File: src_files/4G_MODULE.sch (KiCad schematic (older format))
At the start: 28 parts

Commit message: schematic capture complete
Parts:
- removed AE? (x2): Antenna_Shield, symbol Device:Antenna_Shield
- added J12: DEBUG_4G, Connector_PinHeader_2.54mm:PinHeader_1x02_P2.54mm_Vertical, symbol Connector:Conn_01x02_Male
- added J13, J14: U.FL-R-SMT-1(10), greencharge-footprints:HRS_U.FL-R-SMT-1(10), symbol U.FL-R-SMT-1_10_:U.FL-R-SMT-1(10)
- C226, C230: renamed from C?; footprint (none) -> Capacitor_SMD:CP_Elec_5x5.4
- C227, C228, C229, C231, C232, C233, C234, C235, C236, C237: renamed from C?; footprint (none) -> Capacitor_SMD:C_0402_1005Metric
- D20: renamed from D?; footprint (none) -> LED_SMD:LED_0603_1608Metric
- J9: renamed from J?; footprint (none) -> greencharge-footprints:MOLEX_78800-0001
- R79, R80, R81, R82, R83: renamed from R?; footprint (none) -> Resistor_SMD:R_0402_1005Metric
- U19: renamed from U?; footprint (none) -> greencharge-footprints:XCVR_EG91EFB-512-SNND
- gave numbers to parts that had none: 6
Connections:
- wire segments 176 -> 182
- no-connect marks 7 -> 59
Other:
- moved on the sheet: C234, C235, C236, C237, R81, R82, R83, U20

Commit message: updated footprint and schematics
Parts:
- removed J12: DEBUG_4G, Connector_PinHeader_2.54mm:PinHeader_1x02_P2.54mm_Vertical, symbol Connector:Conn_01x02_Male
- removed J9: SIM_Card, greencharge-footprints:MOLEX_78800-0001, symbol New_Connector:SIM_Card
- removed U19: quesctel_EG91-EX, greencharge-footprints:XCVR_EG91EFB-512-SNND, symbol GCL_Integrated-Circuits:quesctel_EG91-EX
- added C284, C285: 10nF, Capacitor_SMD:C_0402_1005Metric, symbol Device:C_Small
- added D26: SMF11A, Diode_SMD:D_SOD-123, symbol dk_TVS-Diodes:ESD5Z3_3T1G
- added D27: LED_GREEN, LED_SMD:LED_0603_1608Metric, symbol Device:LED
- added J9: SIM_Card_Shielded, greencharge-footprints:GCT_SIM8066-6-1-14-01-A_REVA, symbol Connector:SIM_Card_Shielded
- added JP1: Jumper, TestPoint:TestPoint_2Pads_Pitch2.54mm_Drill0.8mm, symbol Device:Jumper
- added Q12: DTC143ZEBTL, greencharge-footprints:SOTFL50P160X85-3N, symbol DTC143ZEBTL:DTC143ZEBTL
- added R106, R107, R108: 4.7K, Resistor_SMD:R_0402_1005Metric, symbol Device:R_US
- added R109: 0R, Resistor_SMD:R_0402_1005Metric, symbol Device:R_US
- added TP20, TP21: DBG_RXD, TestPoint:TestPoint_Pad_2.0x2.0mm, symbol Connector:TestPoint
- added U19: EG25G, greencharge-footprints:XCVR_EG25G, symbol EG25G:EG25G
- C226, C230: footprint Capacitor_SMD:CP_Elec_5x5.4 -> Capacitor_Tantalum_SMD:CP_EIA-3216-18_Kemet-A; MPN (none) -> T490A107M006ATE800
- D20: value LED -> LED_GREEN
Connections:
- net labels added: 1.8V_local_ldo, ANT_GNSS_GPS, ANT_MAIN, AP_READY, DBG_RXD, DBG_TXD, Net_status, PWR_EN, RESET_n, Status_indicator, USB_BOOT
- wire segments 182 -> 154
- no-connect marks 59 -> 47
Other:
- note added: "50 ohm IMPEDANCE LINES"
- note added: "ANTENNAS(4G LTE AND GPS)"
- note added: "CODEC_INTERFACE"
- note added: "EG25G 4G(LTE/GSM) AND GPS MODULE"
- note added: "ESD PROTECTION FOR USB LINES"
- note added: "GPS ANTENNA = PASSIVE\nFRQ= 1575.42±1.023"
- note added: "LTE_CAPABLE ANTENNA\nFRQ= TX=1920~1980 \n RX= 2110~2170"
- note added: "MODULE ENABLE CIRCUIT"
- note added: "NANO_SIM_CONNECTOR(8-pins)"
- note added: "NETWORK INDICATOR"
- note added: "RESET CIRCUIT"
- note added: "STATUS INDICATOR\n"
- note added: "Status Indicato"
- note added: "USB BOOT"
- note added: "pull_up"
- note removed: "NOTE: Ensure proper heat decipation"
- moved on the sheet: C226, C227, C228, C229, C230, C231, C232, C233, C234, C235, C236, C237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

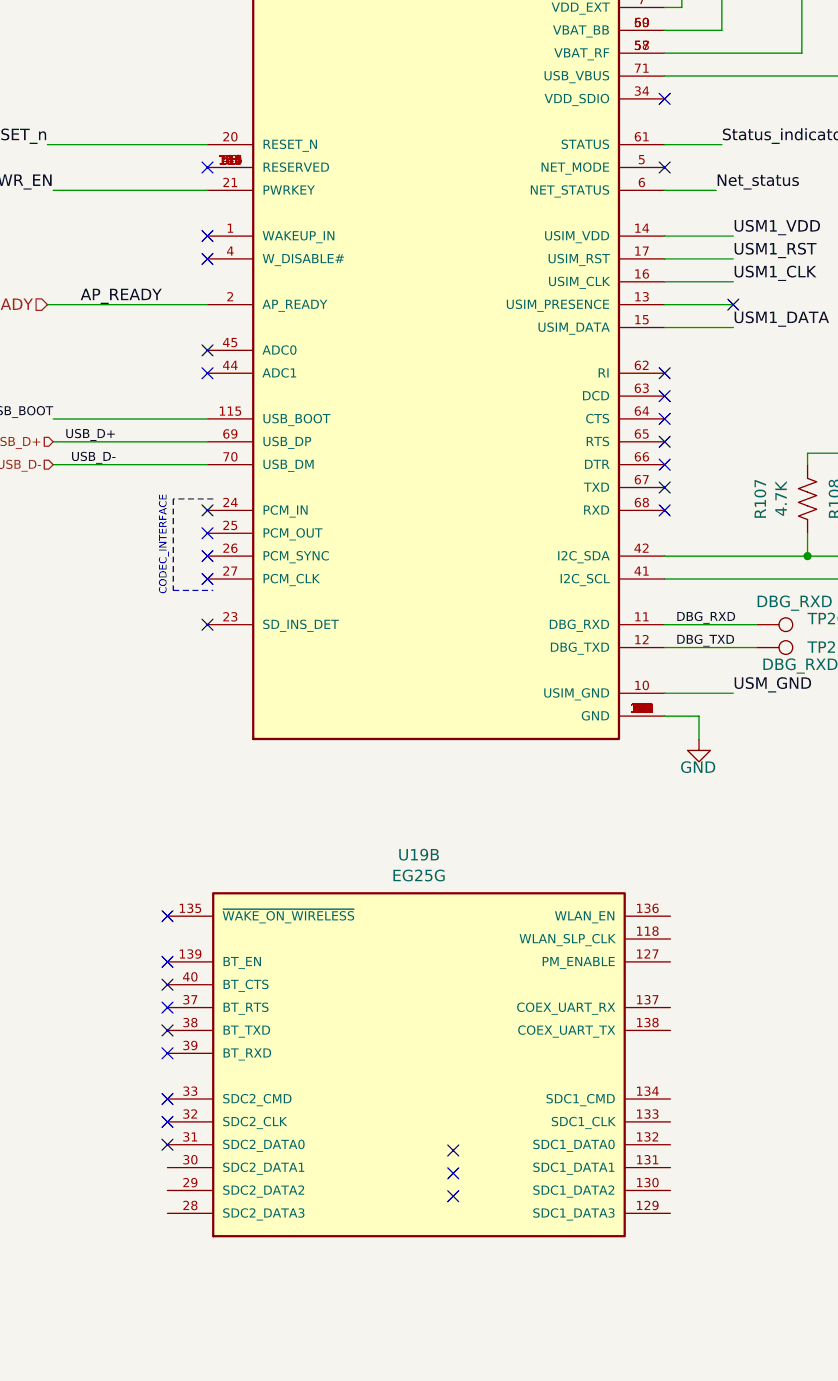
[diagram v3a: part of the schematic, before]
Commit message: complete update on schematic and all display interfaces
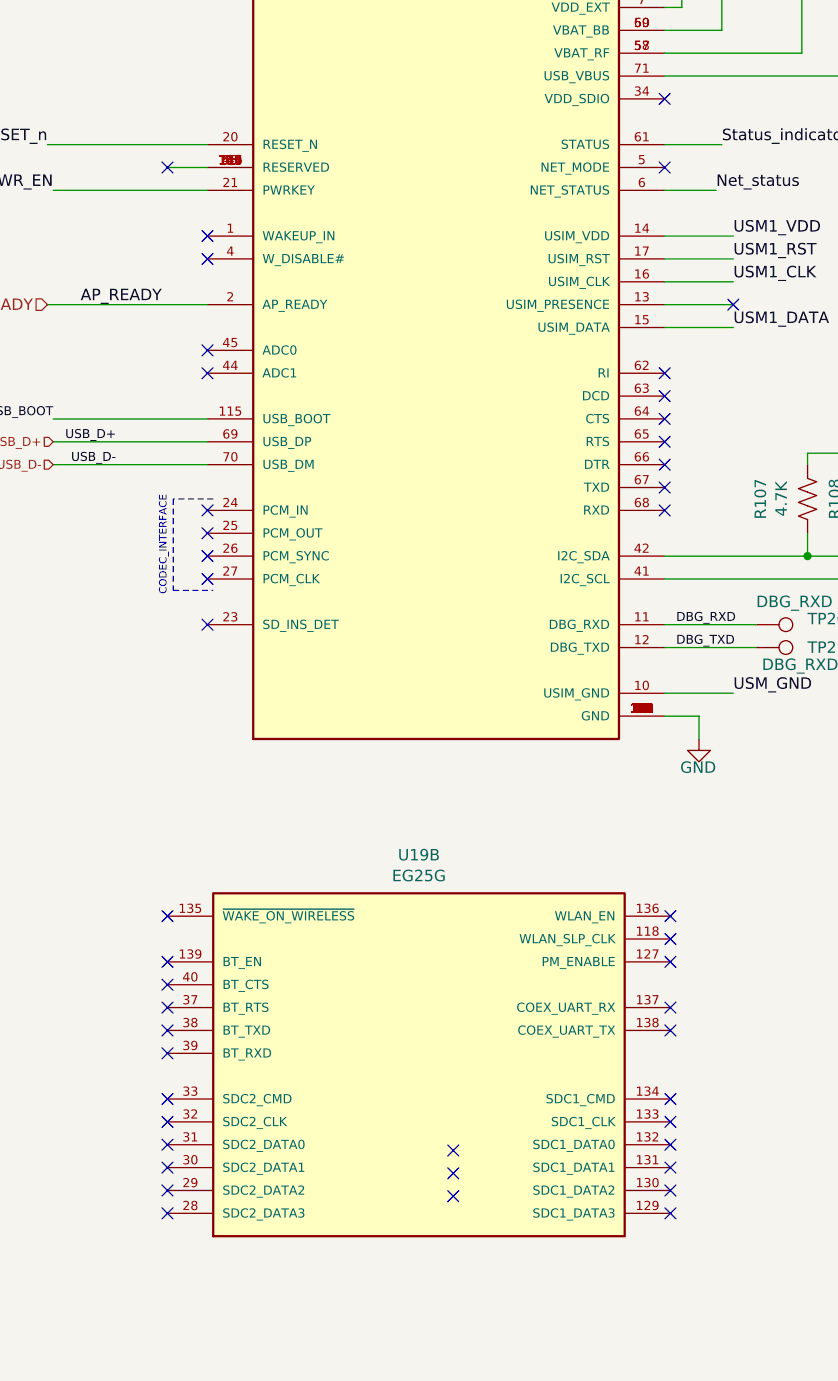
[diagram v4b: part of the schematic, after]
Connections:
- no-connect marks 47 -> 61
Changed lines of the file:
@@
 $Descr A3 16535 11693
 encoding utf-8
-Sheet 15 15
+Sheet 13 15
 Title ""
 Date ""
@@
 Wire Wire Line
 	5475 3300 4800 3300
-NoConn ~ 5475 3200
 Text GLabel 8400 2600 1    33   Input ~ 0
 VCC_3V3
@@
 	0    1    1    0
 $EndComp
+NoConn ~ 7500 6475
+NoConn ~ 7500 6575
+NoConn ~ 7500 6675
+NoConn ~ 7500 6875
+NoConn ~ 7500 6975
+NoConn ~ 7500 7275
+NoConn ~ 7500 7375
+NoConn ~ 7500 7475
+NoConn ~ 7500 7575
+NoConn ~ 7500 7675
+NoConn ~ 7500 7775
+NoConn ~ 5300 7575
+NoConn ~ 5300 7675
+NoConn ~ 5300 7775
+Wire Wire Line
+	5475 3200 5300 3200
+NoConn ~ 5300 3200
 $EndSCHEMATC

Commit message: complete update on schematiC + FOOTPRINT
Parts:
- removed J9: SIM_Card_Shielded, greencharge-footprints:GCT_SIM8066-6-1-14-01-A_REVA, symbol Connector:SIM_Card_Shielded
- added J9: SIM8066-6-1-14-01-A_REVA, greencharge-footprints:GCT_SIM8066-6-1-14-01-A_REVA, symbol SIM8066-6-1-14-01-A_REVA:SIM8066-6-1-14-01-A_REVA
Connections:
- net USM_GND is gone; now on net GND: C236.1, U19.10 (USIM_GND)
- net GND: now also J9.C5 (GND), J9.CD, J9.G1 (GND), J9.G2 (GND), J9.G3 (GND), J9.G4 (GND)
- net USM1_VDD: now also J9.C1 (VCC)
- net at C234.1, R109.1, R81.1: now also J9.C7 (I/O)
- net at C237.1, R82.1: now also J9.C2 (RST)
- net at C235.1, R83.1: now also J9.C3 (CLK)
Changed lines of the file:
@@
 Wire Wire Line
 	7475 3500 7775 3500
-Text Label 12550 7375 2    50   ~ 0
+Text Label 12325 7375 2    50   ~ 0
 USM_GND
 Text Label 12575 7075 2    50   ~ 0
@@
 Wire Wire Line
 	13800 7275 14700 7275
-Wire Wire Line
-	12550 7375 14700 7375
 NoConn ~ 14700 7475
 Wire Wire Line
@@
 Text Notes 12075 6575 0    39   ~ 0
 NOTE: Keep placement of (U)SIM card connector to the module as close as possible. Keep the trace length\nas less than 200mm as possible.\nKeep (U)SIM card signals away from RF and VBAT traces.\nMINIMIZE cross talk.
-$Comp
-L Connector:SIM_Card_Shielded J9
-U 1 1 6305C88F
-P 15200 7375
-F 0 "J9" H 15275 6900 50  0000 L CNN
-F 1 "SIM_Card_Shielded" H 14925 6800 50  0000 L CNN
-F 2 "greencharge-footprints:GCT_SIM8066-6-1-14-01-A_REVA" H 15200 7725 50  0001 C CNN
-F 3 " ~" H 15150 7375 50  0001 C CNN
-	1    15200 7375
-	1    0    0    -1
-$EndComp
 Wire Wire Line
 	14575 7675 14575 8275
@@
 	5475 3200 5300 3200
 NoConn ~ 5300 3200
+$Comp
+L SIM8066-6-1-14-01-A_REVA:SIM8066-6-1-14-01-A_REVA J9
+U 1 1 6EC1A329
+P 15100 7375
+F 0 "J9" H 15330 7421 50  0000 L CNN
+F 1 "SIM8066-6-1-14-01-A_REVA" H 14625 7850 50  0000 L CNN
+F 2 "greencharge-footprints:GCT_SIM8066-6-1-14-01-A_REVA" H 15100 7375 50  0001 L BNN
+F 3 "" H 15100 7375 50  0001 L BNN
+F 4 "Manufacturer recommendations" H 15100 7375 50  0001 L BNN "STANDARD"
+F 5 "1.44mm" H 15100 7375 50  0001 L BNN "MAXIMUM_PACKAGE_HEIGHT"
+F 6 "Global Connector Technology" H 15100 7375 50  0001 L BNN "MANUFACTURER"
+F 7 "REVA" H 15100 7375 50  0001 L BNN "PARTREV"
+	1    15100 7375
+	1    0    0    -1
+$EndComp
+$Comp
+L OLIMEX_Power:GND #PWR0375
+U 1 1 6EC376D6
+P 11950 7400
+F 0 "#PWR0375" H 11950 7150 50  0001 C CNN
+F 1 "GND" H 11955 7227 50  0000 C CNN
+F 2 "" H 11950 7400 60  0000 C CNN
+F 3 "" H 11950 7400 60  0000 C CNN
+	1    11950 7400
+	1    0    0    -1
+$EndComp
+Wire Wire Line
+	11950 7375 11950 7400
+Wire Wire Line
+	11950 7375 14700 7375
 $EndSCHEMATC
